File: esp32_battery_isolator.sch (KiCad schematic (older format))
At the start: 63 parts, among them J1 BATT1, J2 Conn_01x04_Female, J3 USB_B_Micro, J4 BATT2, J5 LOAD1, J6 CHGR, J7 LOAD2, J8 LOAD3, Q10 AP6679GH-HF, Q2 AP6679GH-HF, Q4 AP6679GH-HF, Q6 AP6679GH-HF, Q8 AP6679GH-HF, SW1 C492887, SW2 C492887, SW3 C492887, U1 ESP32-WROOM-32D, U2 LM317AG-TN3-R, U3 ADC128D818, U4 CC6903SO-30A, U5 CH330N, U6 CC6903SO-30A

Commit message: WIP
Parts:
- added D5, D6: SS52, Diode_SMD:D_SMB, symbol Diode:B220
- added D7, D8, D9: 1N4148WS, Diode_SMD:D_SOD-323, symbol Diode:1N4148WS
- added Q1, Q3, Q5, Q7, Q9: MMBT3904, Package_TO_SOT_SMD:SOT-23, symbol Transistor_BJT:MMBT3904
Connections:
- wire segments 115 -> 121
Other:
- note added: "Body diode protection"
- note added: "RTC_GPIO10"
- note added: "RTC_GPIO14"
- note removed: "RTC_GPIO11"
- moved on the sheet: J1, J4, J5, J6, J7, J8, Q4, Q6, R14, R15, R2, R3

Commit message: REV D Complete - Off to JLCPCB for assembly!
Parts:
- removed D5: SS52, Diode_SMD:D_SMB, symbol Diode:B220
- added J9: Conn_01x02_Male, Connector_JST:JST_XH_B2B-XH-A_1x02_P2.50mm_Vertical, symbol Connector:Conn_01x02_Male
- added Q11: AP6679GH, Acea:TRANS_AONR21321, symbol Transistor_FET:QM6015D
- added Q12: MMBT3904, Package_TO_SOT_SMD:SOT-23, symbol Transistor_BJT:MMBT3904
- Q4: value AP6679GH-HF -> AP6679GH; footprint Package_TO_SOT_SMD:TO-252-2 -> Acea:TRANS_AONR21321; lcsc_part_number C124530 -> C431196; lcsc_url https://lcsc.com/product-detail/MOSFET_Advanced-Power-Elec-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 -> (none); package TO-252-2 -> DFN 3x3
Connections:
- net labels added: FANGND, FANON
- wire segments 121 -> 127
- no-connect marks 24 -> 23
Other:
- note added: "12V FAN"
- note added: "FAN PWM"
- moved on the sheet: C10, C9, U5

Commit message: committing
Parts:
- removed C11, C3: 1uF, Capacitor_Tantalum_SMD:CP_EIA-3528-21_Kemet-B, symbol Device:CP_Small
- removed D1, D3, D4: MAIN LED, LED_SMD:LED_0603_1608Metric, symbol Device:LED
- removed D2: SS14, Diode_SMD:D_SMA, symbol Device:D_Schottky_Small
- removed D6: SS52, Diode_SMD:D_SMB, symbol Diode:B220
- removed D7: 1N4148WS, Diode_SMD:D_SOD-323, symbol Diode:1N4148WS
- removed R25: 200R, Resistor_SMD:R_0603_1608Metric, symbol Device:R_Small
- removed R26: 330R, Resistor_SMD:R_0603_1608Metric, symbol Device:R_Small
- removed R5: 3.6k, Resistor_SMD:R_0603_1608Metric, symbol Device:R_Small
- removed SW3: C492887, Acea:TS4550TP, symbol MAX17260:TACT-SWITCH
- removed U2: LM317AG-TN3-R, Package_TO_SOT_SMD:TO-252-2, symbol Regulator_Linear:LM317_TO-252
- added C11: 33p, Capacitor_SMD:C_0603_1608Metric, symbol Device:C_Small
- added C13: 100n, Capacitor_SMD:C_0603_1608Metric, symbol Device:C_Small
- added C14: 10u, Capacitor_SMD:C_0805_2012Metric, symbol Device:C_Small
- added C15: 4.7u, Capacitor_SMD:C_0805_2012Metric, symbol Device:C_Small
- added C8: 4.7, Capacitor_SMD:C_0805_2012Metric, symbol Device:C_Small
- added D1, D2, D3: B5819W, Diode_SMD:D_SOD-123, symbol Diode:1N4148WS
- added L1: L_Small, Inductor_SMD:L_Taiyo-Yuden_NR-30xx, symbol Device:L_Small
- added Q13: AONR21321, Acea:TRANS_AONR21321, symbol Transistor_FET:QM6015D
- added R27, R28, R29, R30, R31: 510R, Resistor_SMD:R_0603_1608Metric, symbol Device:R_Small
- added U7: BL9342, Package_TO_SOT_SMD:SOT-23-6, symbol Relay:BL9342
- D8, D9: value 1N4148WS -> B5819W; footprint Diode_SMD:D_SOD-323 -> Diode_SMD:D_SOD-123; lcsc_part_number C2128 -> C8598; lcsc_url https://lcsc.com/product-detail/Switching-Diode_Changjiang-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 -> (none); mfr_part_number 1N4148WS -> (none)
- J9: value Conn_01x02_Male -> Conn_01x03_Male; footprint Connector_JST:JST_XH_B2B-XH-A_1x02_P2.50mm_Vertical -> Connector_JST:JST_SH_SM03B-SRSS-TB_1x03-1MP_P1.00mm_Horizontal; symbol Connector:Conn_01x02_Male -> Connector:Conn_01x03_Male; lcsc_part_number C20079 -> C160403
- Q10, Q2, Q6, Q8: value AP6679GH-HF -> AONR21321; footprint Package_TO_SOT_SMD:TO-252-2 -> Acea:TRANS_AONR21321; lcsc_part_number C124530 -> C431196; lcsc_url https://lcsc.com/product-detail/MOSFET_Advanced-Power-Elec-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 -> (none); package TO-252-2 -> DFN 3x3
- Q11, Q4: value AP6679GH -> AONR21321
- R2: value 3.6k -> 124k; lcsc_part_number C22980 -> C22788; lcsc_url https://lcsc.com/product-detail/Chip-Resistor-Surface-Mount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 -> (none); package 0603 -> (none)
- R3: value 3.6k -> 40.2k; lcsc_part_number C22980 -> C12447; lcsc_url https://lcsc.com/product-detail/Chip-Resistor-Surface-Mount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 -> (none); package 0603 -> (none)
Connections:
- net labels added: RPM
- net labels removed: B1_LED, B2_LED, SYS_OK_LED
- wire segments 127 -> 155
- no-connect marks 23 -> 25
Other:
- note added: "DC-DC Buck (40V to 3.3V 600mA)"
- note added: "RTC_17"
- note removed: "17"
- note removed: "Body diode protection"
- note removed: "DC-DC Buck (30V, 3.3V, 1.5A)"
- note removed: "Status LEDS\n"
- moved on the sheet: C2, J6, Q9, R20

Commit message: REV E - shipped to JLCPCB
Good to go for JLCPCB assembly service
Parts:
- C15: value 4.7u -> 4.7uF
- C8: value 4.7 -> 4.7uF
- U4, U6: symbol Sensor_Current:CC6903-30A -> esp32_battery_isolator-rescue:CC6903-30A-Sensor_Current
- U7: symbol Relay:BL9342 -> esp32_battery_isolator-rescue:BL9342-Relay; lcsc_part_number (none) -> C93176
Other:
- moved on the sheet: D3, D8, D9, J5, J7, J8, Q10, Q2, Q3, Q7, Q8, Q9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

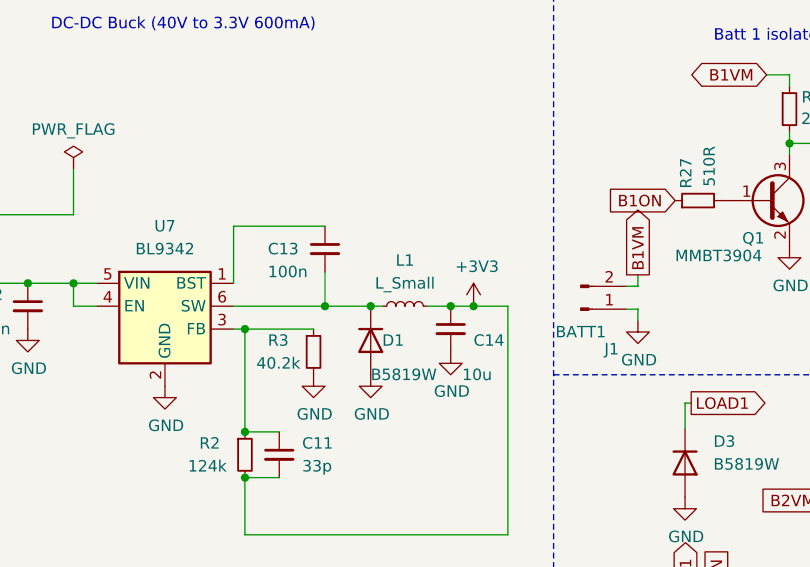
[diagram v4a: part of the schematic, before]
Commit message: REV F - WIP fixed ground plane issuer around SMPS
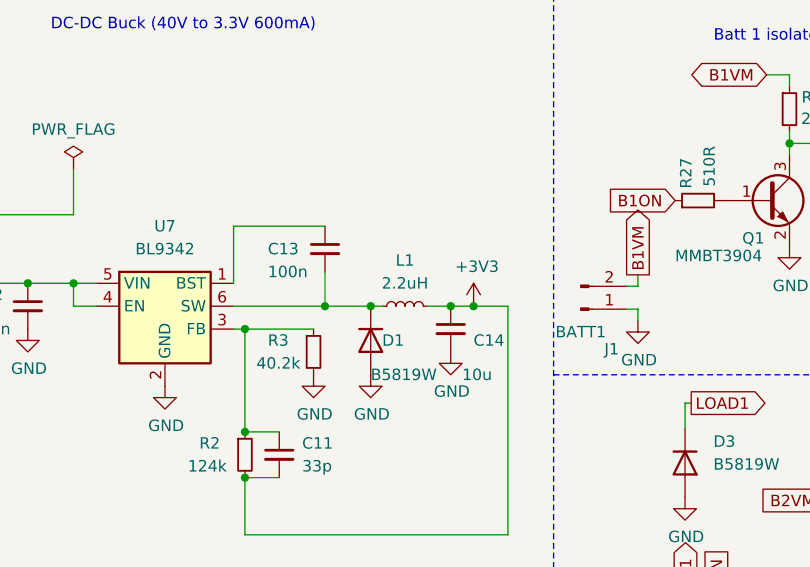
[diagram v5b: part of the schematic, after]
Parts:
- L1: value L_Small -> 2.2uH
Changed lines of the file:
@@
 P 2850 1900
 F 0 "L1" V 3050 1900 50  0000 C CNN
-F 1 "L_Small" V 2950 1900 50  0000 C CNN
+F 1 "2.2uH" V 2950 1900 50  0000 C CNN
 F 2 "Inductor_SMD:L_Taiyo-Yuden_NR-30xx" H 2850 1900 50  0001 C CNN
 F 3 "~" H 2850 1900 50  0001 C CNN

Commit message: REV F - WIP
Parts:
- removed C11: 33p, Capacitor_SMD:C_0603_1608Metric, symbol Device:C_Small
- removed C13: 100n, Capacitor_SMD:C_0603_1608Metric, symbol Device:C_Small
- removed C14: 10u, Capacitor_SMD:C_0805_2012Metric, symbol Device:C_Small
- removed C8: 4.7uF, Capacitor_SMD:C_0805_2012Metric, symbol Device:C_Small
- removed D1: B5819W, Diode_SMD:D_SOD-123, symbol Diode:1N4148WS
- removed U7: BL9342, Package_TO_SOT_SMD:SOT-23-6, symbol esp32_battery_isolator-rescue:BL9342-Relay
- added C3: 220uF, Capacitor_SMD:C_Elec_6.3x7.7, symbol Device:CP_Small
- added C8: 220uF, Capacitor_Tantalum_SMD:CP_EIA-3528-15_AVX-H, symbol Device:CP_Small
- added D1: SS34, Diode_SMD:D_SMA, symbol Device:D_Small
- added D4: LED_Small, LED_SMD:LED_0603_1608Metric, symbol Device:LED_Small
- added R25, R26, R32, R33, R5: 11k, Resistor_SMD:R_0603_1608Metric, symbol Device:R_Small
- added U2: XL1509_SOP8, Package_SO:SOIC-8_3.9x4.9mm_P1.27mm, symbol xl1509_sop8:XL1509_SOP8
- C2: value 100n -> 10nF; lcsc_part_number C14663 -> C57112; lcsc_url https://lcsc.com/product-detail/Multilayer-Ceramic-Capacito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 -> (none); package 0603 -> (none)
- L1: value 2.2uH -> 47uH; footprint Inductor_SMD:L_Taiyo-Yuden_NR-30xx -> Inductor_SMD:L_Bourns_SRN6045TA; lcsc_part_number C167747 -> C36414
- R2: value 124k -> 11k; lcsc_part_number C22788 -> C25950; lcsc_url (none) -> https://lcsc.com/product-detail/Chip-Resistor-Surface-Mount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; package (none) -> 0603
- R3: value 40.2k -> 3.6k; lcsc_part_number C12447 -> C22980; lcsc_url (none) -> https://lcsc.com/product-detail/Chip-Resistor-Surface-Mount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; package (none) -> 0603
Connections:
- net +3V3: now also C8.1, D1.1 (K), U2.2 (SW); no longer R2.2, R9.2
- net B2VM: now also R2.2, C3.1, U2.1 (VIN)
- net BOOT: no longer R9.1
- net FANON: now also R32.1
- net GND: now also R9.2, C3.2, C8.2, D1.2 (A), D4.1 (K), R25.2, R26.2, R32.2, R33.2, R5.2, U2.5 (GND), U2.6 (GND), U2.7 (GND), U2.8 (GND); no longer R3.2
- net SYS_LED: now reaches U1.37 (IO23)
- net SYS_LED: now also R3.1
- net at Q1.1 (B), R27.2: now also R5.1
- net at Q5.1 (B), R29.2: now also R25.1
- net at Q3.1 (B), R28.2: now also R9.1
- net at Q7.1 (B), R30.2: now also R26.1
- net at Q9.1 (B), R31.2: now also R33.1
- net at R2.1: now also U2.4 (~EN); no longer R3.1
- net at L1.1: now also U2.3 (FB)
- new net: D4.2 (A), R3.2
- no-connect marks 25 -> 24
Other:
- moved on the sheet: D2, J4, J7, Q13, Q5, Q6, R15, R27, R28, R29, R30, R31

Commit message: REV F - off to JLCPCB
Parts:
- Q10, Q11, Q13, Q2, Q4, Q6, Q8: footprint Acea:TRANS_AONR21321 -> Acea:DFN-TRANS_AONR21321
- U5: value CH330N -> CH340N; lcsc_part_number C108996 -> C506813; lcsc_url https://lcsc.com/product-detail/USB-ICs_WCH-Jiangsu-Qin-Hen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 -> (none); mfr_part_number CH330N -> CH340N
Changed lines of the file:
@@
 Sheet 1 1
 Title "ESP32 Battery Isolator"
-Date "2021-08-04"
-Rev "E"
+Date "2021-09-02"
+Rev "F"
 Comp "Acea Quigg"
 Comment1 ""
@@
 Text GLabel 10900 4550 2    50   Input ~ 0
 RXD
-Text Notes 1950 4400 0    50   ~ 0
+Text Notes 1966 3855 0    50   ~ 0
 ESP-32
 Wire Notes Line
@@
 P 10500 4650
 F 0 "U5" H 10145 5150 50  0000 C CNN
-F 1 "CH330N" H 10250 5055 50  0000 C CNN
+F 1 "CH340N" H 10250 5055 50  0000 C CNN
 F 2 "Package_SO:SOIC-8_3.9x4.9mm_P1.27mm" H 10350 5400 50  0001 C CNN
-F 3 "https://datasheet.lcsc.com/szlcsc/1811151442_WCH-Jiangsu-Qin-Heng-CH330N_C108996.pdf" H 10400 4850 50  0001 C CNN
-F 4 "C108996" H 10500 4650 50  0001 C CNN "lcsc_part_number"
-F 5 "https://lcsc.com/product-detail/USB-ICs_WCH-Jiangsu-Qin-Heng-CH330N_C108996.html" H 10500 4650 50  0001 C CNN "lcsc_url"
-F 6 "1" H 10500 4650 50  0001 C CNN "lcsc_min_qty"
-F 7 "CH330N" H 10500 4650 50  0001 C CNN "mfr_part_number"
-F 8 "SOP-8" H 10500 4650 50  0001 C CNN "package"
+F 3 "" H 10400 4850 50  0001 C CNN
+F 4 "C506813" H 10500 4650 50  0001 C CNN "lcsc_part_number"
+F 5 "1" H 10500 4650 50  0001 C CNN "lcsc_min_qty"
+F 6 "CH340N" H 10500 4650 50  0001 C CNN "mfr_part_number"
+F 7 "SOP-8" H 10500 4650 50  0001 C CNN "package"
 	1    10500 4650
 	1    0    0    -1
@@
 Text GLabel 2871 4420 0    50   Input ~ 0
 MODE
-Text GLabel 3400 7000 2    50   Input ~ 0
+Text GLabel 2700 7000 2    50   Input ~ 0
 MODE
 Wire Wire Line
@@
 Wire Wire Line
 	10162 3285 10212 3285
-Text GLabel 9203 3284 1    50   Input ~ 0
+Text GLabel 9203 3262 1    50   Input ~ 0
 L3ON
 Wire Wire Line
@@
 Wire Wire Line
 	9308 3285 9203 3285
-Wire Wire Line
-	9203 3285 9203 3284
 NoConn ~ 2700 6700
 NoConn ~ 2700 6800
@@
 F 0 "Q2" H 5192 3241 50  0000 L CNN
 F 1 "AONR21321" H 5199 3160 50  0000 L CNN
-F 2 "Acea:TRANS_AONR21321" H 5200 3024 50  0001 L CIN
+F 2 "Acea:DFN-TRANS_AONR21321" H 5200 3024 50  0001 L CIN
 F 3 "" H 5000 3099 50  0001 L CNN
 F 4 "C431196" H 5000 3099 50  0001 C CNN "lcsc_part_number"
@@
 F 0 "Q8" H 7742 3242 50  0000 L CNN
 F 1 "AONR21321" H 7749 3161 50  0000 L CNN
-F 2 "Acea:TRANS_AONR21321" H 7750 3025 50  0001 L CIN
+F 2 "Acea:DFN-TRANS_AONR21321" H 7750 3025 50  0001 L CIN
 F 3 "" H 7550 3100 50  0001 L CNN
 F 4 "C431196" H 7550 3100 50  0001 C CNN "lcsc_part_number"
@@
 F 0 "Q10" H 10254 3227 50  0000 L CNN
 F 1 "AONR21321" H 10261 3146 50  0000 L CNN
-F 2 "Acea:TRANS_AONR21321" H 10262 3010 50  0001 L CIN
+F 2 "Acea:DFN-TRANS_AONR21321" H 10262 3010 50  0001 L CIN
 F 3 "" H 10062 3085 50  0001 L CNN
 F 4 "C431196" H 10062 3085 50  0001 C CNN "lcsc_part_number"
@@
 F 0 "Q6" H 7253 1709 50  0000 L CNN
 F 1 "AONR21321" H 7260 1628 50  0000 L CNN
-F 2 "Acea:TRANS_AONR21321" H 7261 1492 50  0001 L CIN
+F 2 "Acea:DFN-TRANS_AONR21321" H 7261 1492 50  0001 L CIN
 F 3 "" H 7061 1567 50  0001 L CNN
 F 4 "C431196" H 7061 1567 50  0001 C CNN "lcsc_part_number"
@@
 F 0 "Q4" H 5089 1791 50  0000 L CNN
 F 1 "AONR21321" H 5096 1710 50  0000 L CNN
-F 2 "Acea:TRANS_AONR21321" H 5097 1574 50  0001 L CIN
+F 2 "Acea:DFN-TRANS_AONR21321" H 5097 1574 50  0001 L CIN
 F 3 "" H 4897 1649 50  0001 L CNN
 F 4 "C431196" H 4897 1649 50  0001 C CNN "lcsc_part_number"
@@
 F 0 "Q11" H 5089 1391 50  0000 L CNN
 F 1 "AONR21321" H 5096 1310 50  0000 L CNN
-F 2 "Acea:TRANS_AONR21321" H 5097 1174 50  0001 L CIN
+F 2 "Acea:DFN-TRANS_AONR21321" H 5097 1174 50  0001 L CIN
 F 3 "" H 4897 1249 50  0001 L CNN
 F 4 "C431196" H 4897 1249 50  0001 C CNN "lcsc_part_number"
@@
 F 0 "Q13" H 7253 1309 50  0000 L CNN
 F 1 "AONR21321" H 7260 1228 50  0000 L CNN
-F 2 "Acea:TRANS_AONR21321" H 7261 1092 50  0001 L CIN
+F 2 "Acea:DFN-TRANS_AONR21321" H 7261 1092 50  0001 L CIN
 F 3 "" H 7061 1167 50  0001 L CNN
 F 4 "C431196" H 7061 1167 50  0001 C CNN "lcsc_part_number"
@@
 Text GLabel 1950 1150 2    50   Input ~ 0
 B2VM
-Wire Wire Line
-	2700 7000 3400 7000
 Text GLabel 2700 6500 2    50   Output ~ 0
 SYS_LED
@@
 	8572 4550 8600 4550
 Connection ~ 8600 4550
+Wire Wire Line
+	9203 3262 9203 3285
 $EndSCHEMATC

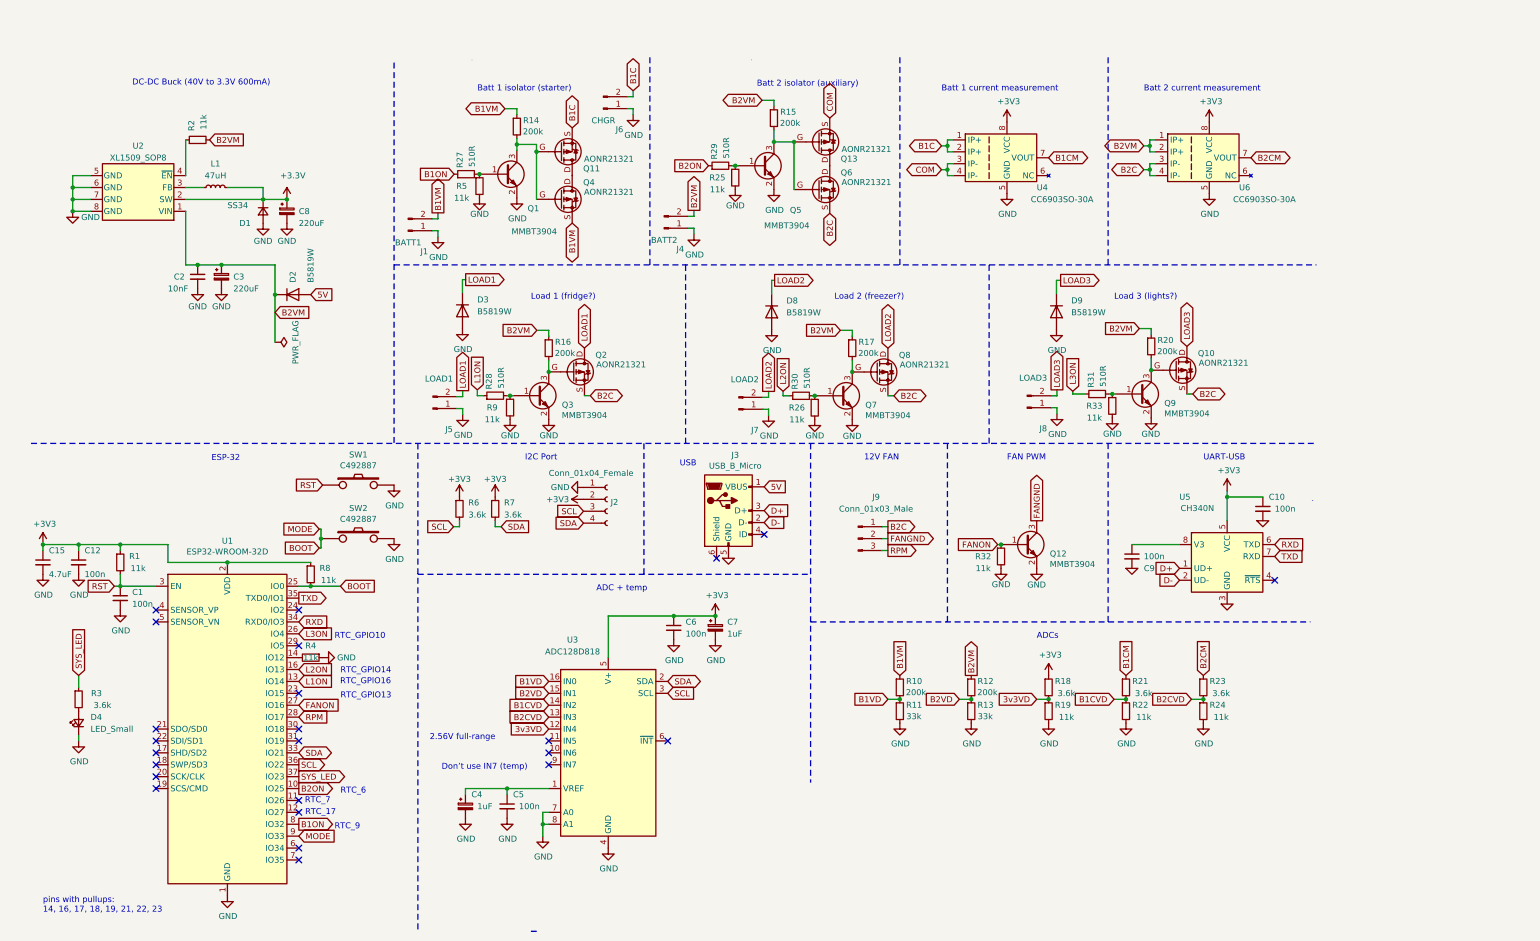
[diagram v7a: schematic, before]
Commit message: Getting closer to finished
Big changes to the app to make it simpler
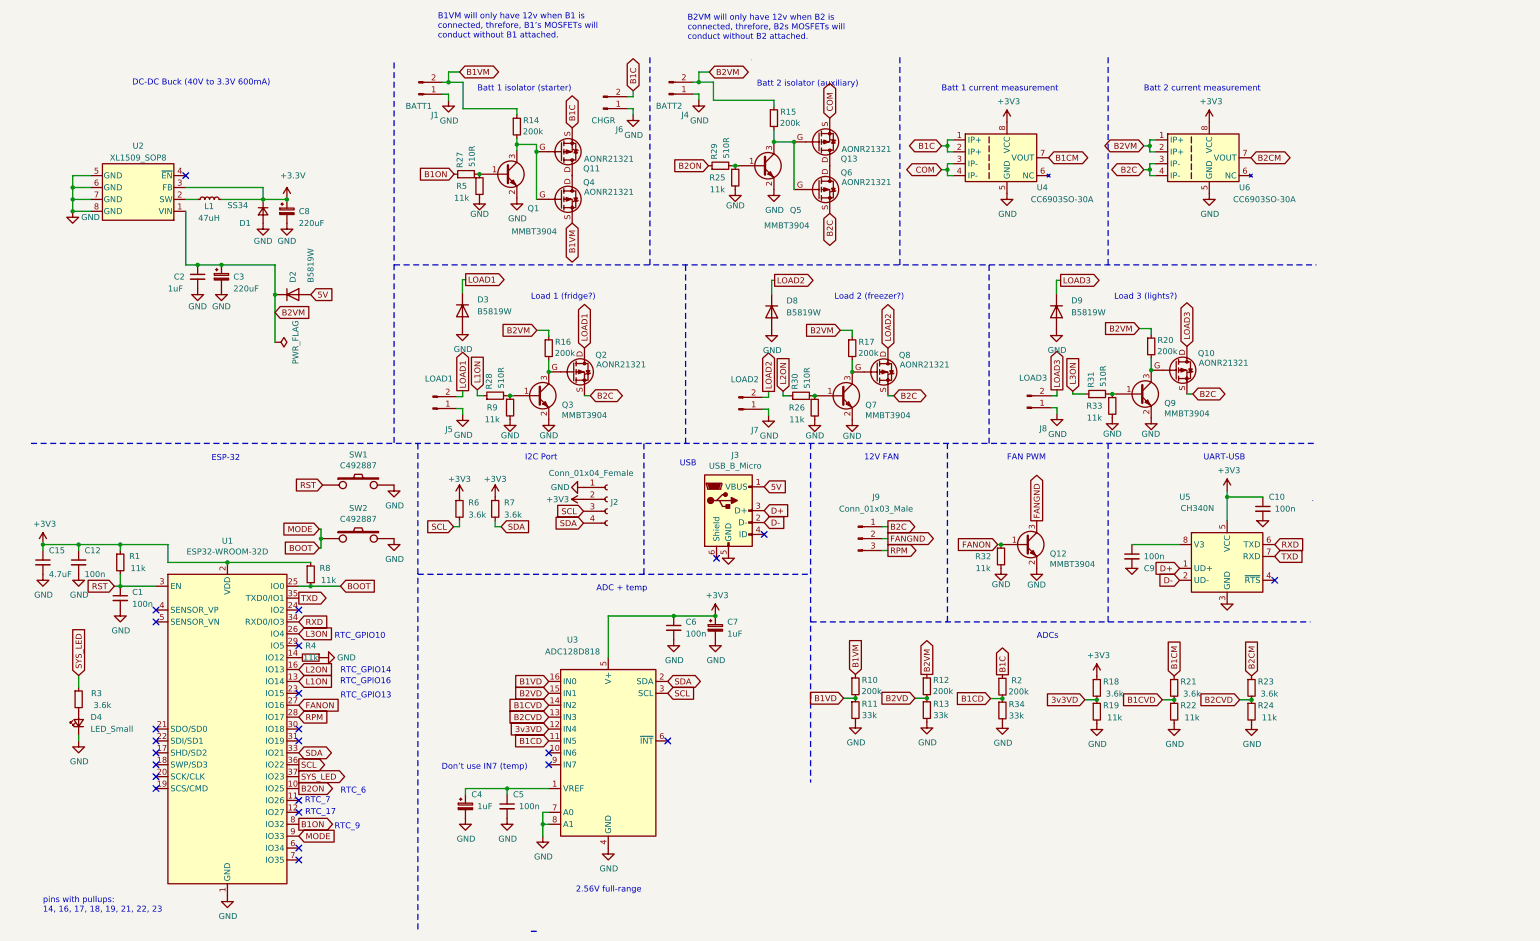
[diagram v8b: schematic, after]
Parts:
- added R34: 33k, Resistor_SMD:R_0603_1608Metric, symbol Device:R_Small
- C2: value 10nF -> 1uF; lcsc_part_number C57112 -> C15849
- R2: value 11k -> 200k; lcsc_part_number C25950 -> C25811; lcsc_url https://lcsc.com/product-detail/Chip-Resistor-Surface-Mount_Uniroyal-Elec-0603WAF1102T5E_C25950.html/?href=jlc-SMT -> https://lcsc.com/product-detail/Chip-Resistor-Surface-Mount_Uniroyal-Elec-0603WAF2003T5E_C25811.html/?href=jlc-SMT
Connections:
- net +3V3: now also U2.3 (FB); no longer U2.2 (SW)
- net B1C: now also R2.1
- net B2VM: no longer R2.2
- net GND: now also R34.2
- net B1CD: now reaches U3.11 (IN5)
- net B1CD: now also R2.2, R34.1
- net at L1.1: now also U2.2 (SW); no longer U2.3 (FB)
- net at U2.4 (~EN): no longer R2.1
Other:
- note added: "B1VM will only have 12v when B1 is \nconnected, threfore, B1’s MOSFETs will \nconduct without B1 attached."
- note added: "B2VM will only have 12v when B2 is \nconnected, threfore, B2s MOSFETs will \nconduct without B2 attached."
- moved on the sheet: J1, J4, L1, R10, R11, R12, R13, R18, R19, R21, R22, R23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
